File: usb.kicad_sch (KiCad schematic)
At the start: 9 parts, among them J1 USB_C_Receptacle_USB2.0_16P, U5 USBLC6-2SC6

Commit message: yeah
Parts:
- added C53: 100n, symbol Device:C
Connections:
- net GND: now also C53.2
- net VBUS_MON: now also C53.1
- net CC1: now reaches J1.A5 (CC1), R3.1
- net CC2: now reaches J1.B5 (CC2), R2.1
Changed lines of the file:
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@@
+	)
+	(junction
+		(at 181.61 74.93)
+		(diameter 0)
+		(color 0 0 0 0)
 	)
 	(junction
@@
 	)
 	(junction
+		(at 171.45 86.36)
+		(diameter 0)
+		(color 0 0 0 0)
+	)
+	(junction
 		(at 137.16 104.14)
 		(diameter 0)
@@
 	(wire
 		(pts
+			(xy 181.61 74.93) (xy 187.96 74.93)
+		)
+		(stroke
+			(width 0)
+			(type default)
+		)
+	)
+	(wire
+		(pts
+			(xy 171.45 86.36) (xy 181.61 86.36)
+		)
+		(stroke
+			(width 0)
+			(type default)
+		)
+	)
+	(wire
+		(pts
 			(xy 137.16 91.44) (xy 137.16 93.98)
 		)
@@
 	(wire
 		(pts
-			(xy 171.45 74.93) (xy 177.8 74.93)
+			(xy 171.45 74.93) (xy 181.61 74.93)
 		)
 		(stroke
@@
 	(wire
 		(pts
+			(xy 181.61 86.36) (xy 181.61 85.09)
+		)
+		(stroke
+			(width 0)
+			(type default)
+		)
+	)
+	(wire
+		(pts
 			(xy 193.04 111.76) (xy 199.39 111.76)
 		)
@@
 	(wire
 		(pts
-			(xy 171.45 85.09) (xy 171.45 87.63)
+			(xy 171.45 85.09) (xy 171.45 86.36)
 		)
 		(stroke
@@
 	(wire
 		(pts
+			(xy 171.45 86.36) (xy 171.45 87.63)
+		)
+		(stroke
+			(width 0)
+			(type default)
+		)
+	)
+	(wire
+		(pts
 			(xy 149.86 116.84) (xy 149.86 123.19)
 		)
@@
 		(pts
 			(xy 137.16 58.42) (xy 137.16 63.5)
+		)
+		(stroke
+			(width 0)
+			(type default)
+		)
+	)
+	(wire
+		(pts
+			(xy 181.61 74.93) (xy 181.61 77.47)
 		)
 		(stroke
@@
 		)
 	)
+	(label "CC1"
+		(at 133.35 116.84 0)
+		(effects
+			(font
+				(size 1.27 1.27)
+			)
+			(justify left bottom)
+		)
+	)
+	(label "CC2"
+		(at 133.35 119.38 0)
+		(effects
+			(font
+				(size 1.27 1.27)
+			)
+			(justify left bottom)
+		)
+	)
 	(label "USB_PRE_TVS_N"
 		(at 139.7 104.14 0)
@@
 	(hierarchical_label "VBUS_MON"
 		(shape input)
-		(at 177.8 74.93 0)
+		(at 187.96 74.93 0)
 		(effects
 			(font
@@
 					(unit 1)
 				)
+			)
+		)
+	)
+	(symbol
+		(lib_id "Device:C")
+		(at 181.61 81.28 0)
+		(unit 1)
+		(exclude_from_sim no)
+		(in_bom yes)
+		(on_board yes)
+		(dnp no)
+		(fields_autoplaced yes)
+		(property "Reference" "C53"
+			(at 185.42 80.0099 0)
+			(effects
+				(font
+					(size 1.27 1.27)
+				)
+				(justify left)
+			)
+		)
+		(property "Value" "100n"
+			(at 185.42 82.5499 0)
+			(effects
+				(font
+					(size 1.27 1.27)
+				)
+				(justify left)
+			)
+		)
+		(property "Footprint" ""
+			(at 182.5752 85.09 0)
+			(effects
+				(font
+					(size 1.27 1.27)
+				)
+				(hide yes)
+			)
+		)
+		(property "Datasheet" "~"
+			(at 181.61 81.28 0)
+			(effects
+				(font
+					(size 1.27 1.27)
+				)
+				(hide yes)
+			)
+		)
+		(property "Description" "Unpolarized capacitor"
+			(at 181.61 81.28 0)
+			(effects
+				(font
+					(size 1.27 1.27)
+				)
+				(hide yes)
+			)
+		)
+		(pin "2"
+		)
+		(pin "1"
+		)
+		(instances
+			(project "hoppen_fc"
+				(path "/abe950a1-9eef-4508-9fd4-31d3e723e029/c85454e5-a89e-41eb-a5ed-71b4fc4cf13a/70185383-c6d2-4eb6-9764-fd02002b35f8"
+					(reference "C53")
+					(unit 1)
+				)

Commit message: wen branch and pr
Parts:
- R4: value 100k -> 39k
- R5: value 47k -> 10k
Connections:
- net +VBUS: now also D1.1 (A1); no longer D1.2 (A2)
- net GND: now also D1.2 (A2); no longer D1.1 (A1)
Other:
- moved on the sheet: D1
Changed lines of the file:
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@@
+		)
+	)
+	(text_box "DESIGN:\nOutput ~1.02V @ 5V"
+		(exclude_from_sim no)
+		(at 180.34 66.04 0)
+		(size 17.78 5.08)
+		(margins 0.9525 0.9525 0.9525 0.9525)
+		(stroke
+			(width 0.3048)
+			(type solid)
+			(color 132 132 132 1)
+		)
+		(fill
+			(type none)
+		)
+		(effects
+			(font
+				(face "KiCad Font")
+				(size 1.016 1.016)
+			)
+			(justify left top)
 		)
 	)
@@
 		)
 	)
-	(hierarchical_label "USB"
+	(hierarchical_label "{USB}"
 		(shape input)
 		(at 212.09 107.95 0)
@@
 	(symbol
 		(lib_id "0_diodes:SMF5V0A")
-		(at 153.67 74.93 90)
+		(at 153.67 74.93 270)
 		(unit 1)
 		(exclude_from_sim no)
@@
 					(size 1.27 1.27)
 				)
-				(justify right)
+				(justify left)
 			)
 		)
@@
 					(size 1.27 1.27)
 				)
-				(justify right)
+				(justify left)
 			)
 		)
 		(property "Footprint" "Diode_SMD:D_SMF"
-			(at 139.7 74.93 0)
+			(at 167.64 74.93 0)
 			(effects
 				(font
@@
 		)
 		(property "Datasheet" "https://www.vishay.com/doc?85881"
-			(at 144.78 74.93 0)
+			(at 162.56 74.93 0)
 			(effects
 				(font
@@
 		)
 		(property "Description" "200W unidirectional Transil Transient Voltage Suppressor, 5Vrwm, SMF"
-			(at 142.24 74.93 0)
+			(at 165.1 74.93 0)
 			(effects
 				(font
@@
 		)
 		(instances
-			(project ""
+			(project "hoppen_fc"
 				(path "/abe950a1-9eef-4508-9fd4-31d3e723e029/c85454e5-a89e-41eb-a5ed-71b4fc4cf13a/70185383-c6d2-4eb6-9764-fd02002b35f8"
 					(reference "D1")
@@
 			)
 		)
-		(property "Value" "47k"
+		(property "Value" "10k"
 			(at 173.99 82.5499 0)
 			(effects
@@
 			)
 		)
-		(property "Value" "100k"
+		(property "Value" "39k"
 			(at 173.99 69.8499 0)
 			(effects

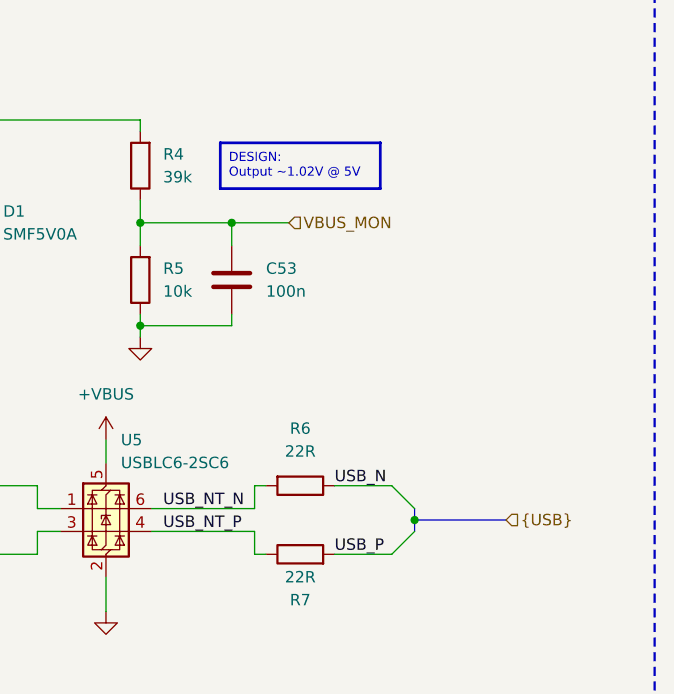
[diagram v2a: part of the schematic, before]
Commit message: much work and .ioc file added
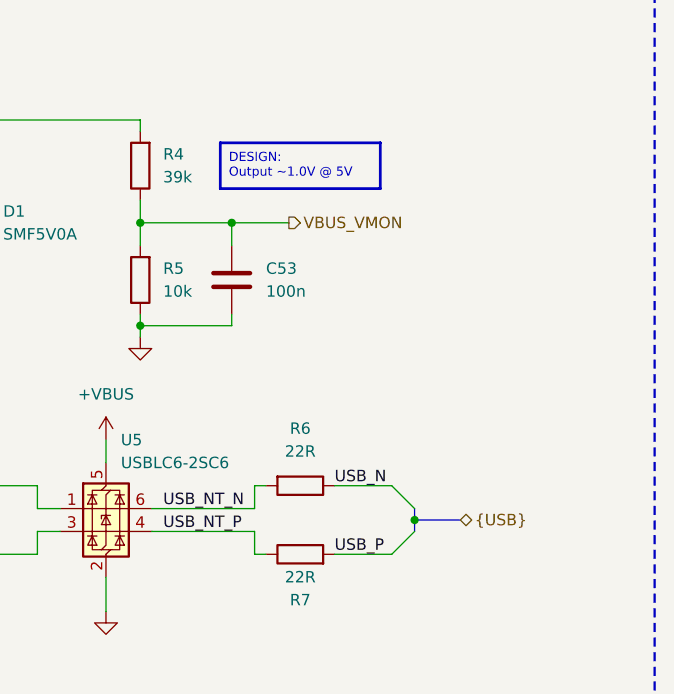
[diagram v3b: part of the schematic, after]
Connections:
- net VBUS_MON renamed VBUS_VMON
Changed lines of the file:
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@@
 		(company "Hoppen")
+	)
+	(bus_alias "USB"
+		(members "USB_N" "USB_P")
 	)
 	(rectangle
@@
 		)
 	)
-	(text_box "DESIGN:\nOutput ~1.02V @ 5V"
+	(text_box "DESIGN:\nOutput ~1.0V @ 5V"
 		(exclude_from_sim no)
 		(at 180.34 66.04 0)
@@
 	(bus
 		(pts
-			(xy 201.93 107.95) (xy 212.09 107.95)
+			(xy 201.93 107.95) (xy 207.01 107.95)
 		)
 		(stroke
@@
 		)
 	)
-	(hierarchical_label "VBUS_MON"
-		(shape input)
+	(hierarchical_label "VBUS_VMON"
+		(shape output)
 		(at 187.96 74.93 0)
 		(effects
@@
 	)
 	(hierarchical_label "{USB}"
-		(shape input)
-		(at 212.09 107.95 0)
-		(effects
-			(font
+		(shape bidirectional)
+		(at 207.01 107.95 0)
+		(effects
+			(font

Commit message: start fix fp
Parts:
- C53: footprint (none) -> 0_capacitor_smd:C_0402_1005Metric
- D1: footprint Diode_SMD:D_SMF -> 0_diodes:D_SMF
- J1: footprint (none) -> 0_connectors:USB-C_SMD-TYPE-C-31-M-12_1; LCSC (none) -> C165948
- R2, R3, R4, R5, R6, R7: footprint (none) -> 0_resistor_smd:R_0402_1005Metric
- U5: footprint Package_TO_SOT_SMD:SOT-23-6 -> 0_diodes:SOT-23-6
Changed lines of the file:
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@@
 			)
 		)
-		(property "Footprint" ""
+		(property "Footprint" "0_resistor_smd:R_0402_1005Metric"
 			(at 148.082 127 90)
 			(effects
@@
 			)
 		)
-		(property "Footprint" ""
+		(property "Footprint" "0_resistor_smd:R_0402_1005Metric"
 			(at 139.192 127 90)
 			(effects
@@
 			)
 		)
-		(property "Footprint" "Package_TO_SOT_SMD:SOT-23-6"
+		(property "Footprint" "0_diodes:SOT-23-6"
 			(at 149.86 85.09 0)
 			(effects
@@
 			)
 		)
-		(property "Footprint" ""
+		(property "Footprint" "0_connectors:USB-C_SMD-TYPE-C-31-M-12_1"
 			(at 118.11 109.22 0)
 			(effects
@@
 			)
 		)
+		(property "LCSC" "C165948"
+			(at 114.3 109.22 0)
+			(effects
+				(font
+					(size 1.27 1.27)
+				)
+				(hide yes)
+			)
+		)
 		(pin "B1"
 		)
@@
 			)
 		)
-		(property "Footprint" ""
+		(property "Footprint" "0_capacitor_smd:C_0402_1005Metric"
 			(at 182.5752 85.09 0)
 			(effects
@@
 			)
 		)
-		(property "Footprint" "Diode_SMD:D_SMF"
+		(property "Footprint" "0_diodes:D_SMF"
 			(at 167.64 74.93 0)
 			(effects
@@
 			)
 		)
-		(property "Footprint" ""
+		(property "Footprint" "0_resistor_smd:R_0402_1005Metric"
 			(at 189.23 102.362 90)
 			(effects
@@
 			)
 		)
-		(property "Footprint" ""
+		(property "Footprint" "0_resistor_smd:R_0402_1005Metric"
 			(at 189.23 113.538 90)
 			(effects
@@
 			)
 		)
-		(property "Footprint" ""
+		(property "Footprint" "0_resistor_smd:R_0402_1005Metric"
 			(at 173.228 81.28 90)
 			(effects
@@
 			)
 		)
-		(property "Footprint" ""
+		(property "Footprint" "0_resistor_smd:R_0402_1005Metric"
 			(at 173.228 68.58 90)
 			(effects
